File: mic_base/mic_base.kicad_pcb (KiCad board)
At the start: 2 copper layers, 50 x 50 mm, 25 parts, among them IC1 1512P08-U, J1 +Power-, J2 +Out-, J3 -Gain+, J4 +Mic In-, U1 NMA0515SC

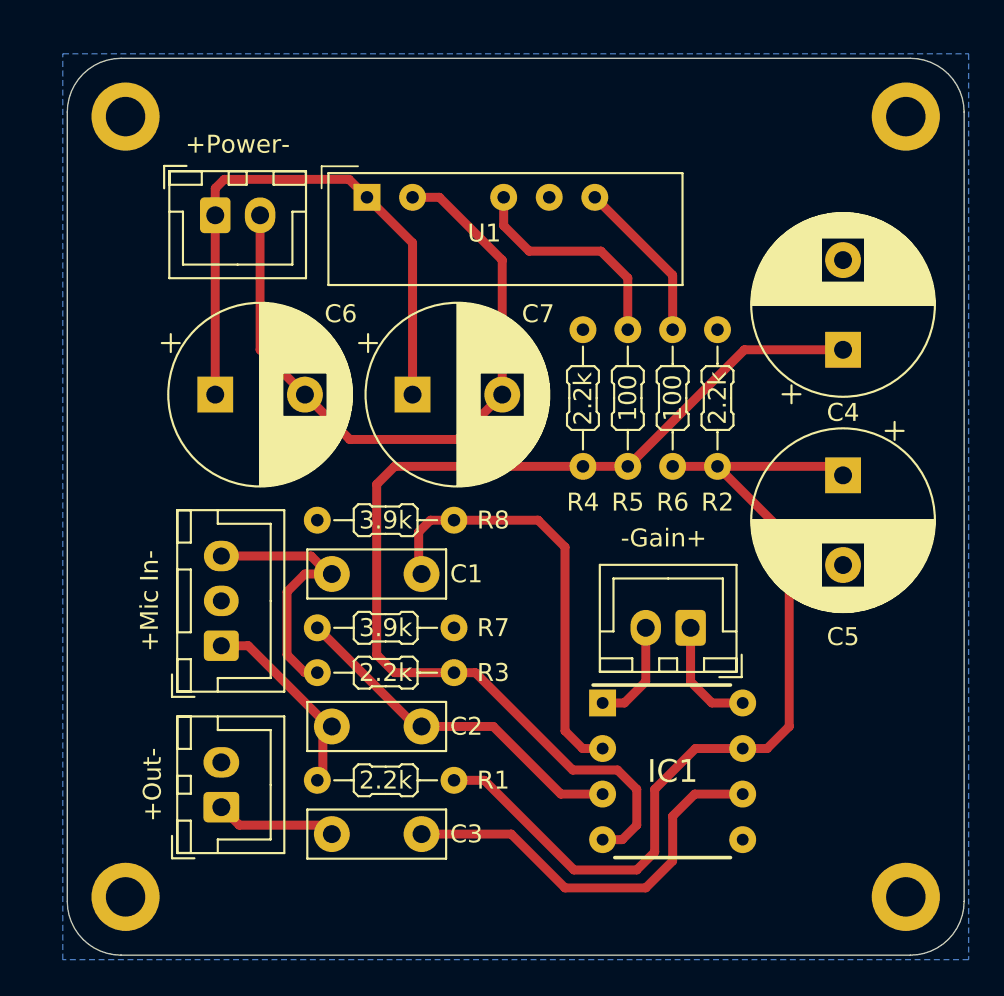
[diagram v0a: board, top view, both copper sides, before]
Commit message: moved capacitors, made pcb smaller
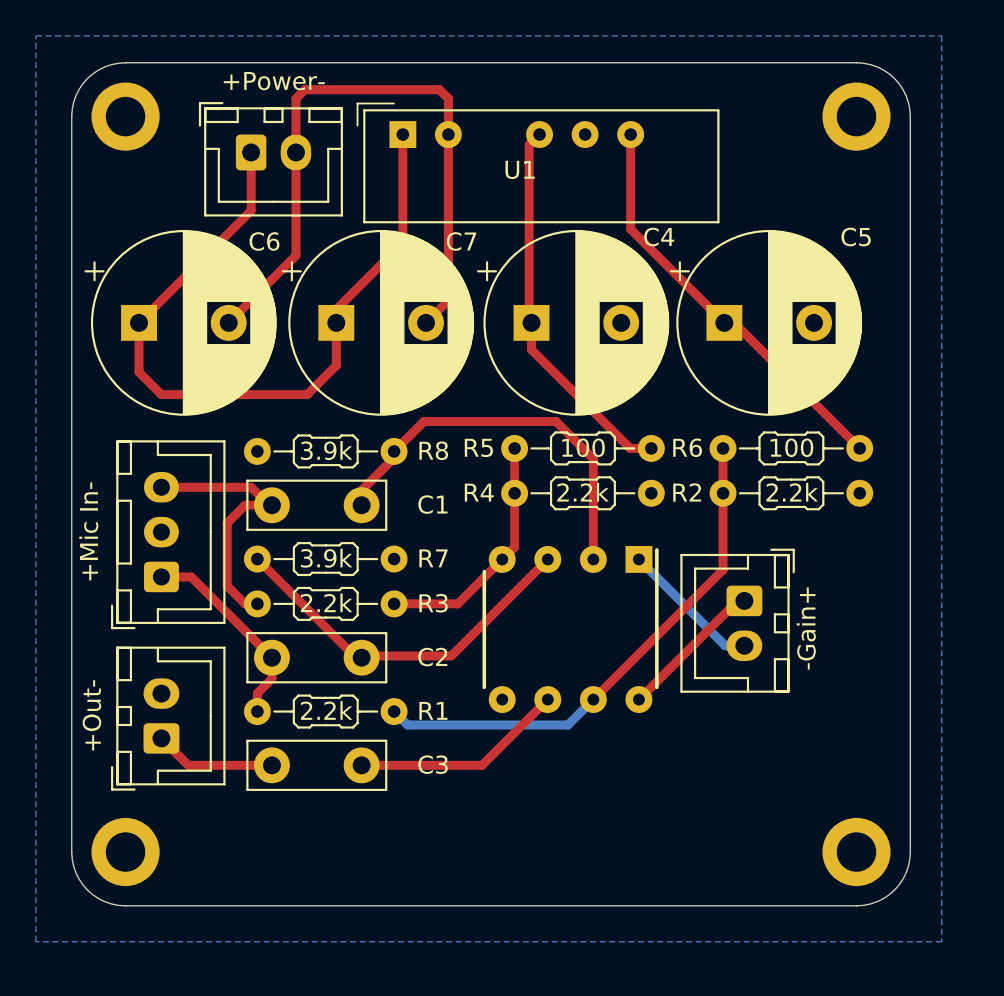
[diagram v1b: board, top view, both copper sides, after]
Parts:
- moved C4 17.4 mm to (104.6, 59.0), turned to 0 degrees
- moved R2 12.1 mm to (122.9, 68.5), turned to 180 degrees
- moved C5 10.8 mm to (115.4, 59.0), turned to 0 degrees
- moved R4 9.88 mm to (111.3, 68.5), turned to 180 degrees
- moved IC1 9.74 mm to (106.8, 76.1), turned to -90 degrees
- moved R5 6.39 mm to (103.7, 66.0), turned to 0 degrees
- moved C6 5.84 mm to (82.8, 59.0)
- moved C7 5.84 mm to (93.8, 59.0)
- moved R8 5.08 mm to (89.3, 66.2)
- moved C1 5.08 mm to (90.2, 69.2)
- moved C2 5.08 mm to (95.2, 77.7)
- moved C3 5.08 mm to (90.2, 83.7)
- moved J2 5.08 mm to (84.0, 82.2)
- moved J4 5.08 mm to (84.0, 73.2)
- moved R1 5.08 mm to (89.4, 80.7)
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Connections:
- C4 pad 1: /-VOut -> Net-(U1-VOUT-)
- C5 pad 1: /+VOut -> Net-(U1-VOUT+)
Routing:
- net /-VOut: track 60.5 -> 13.5 mm
- net /+VOut: track 52.3 -> 29.0 mm
- net Net-(U1-VOUT+): track 9.18 -> 23.1 mm
- net Net-(IC1-OUT): track 22.8 -> 11.9 mm
- net Net-(U1-VOUT-): track 12.6 -> 21.1 mm
- net /+5: track 32.7 -> 40.7 mm
- net /AGND: track 38.6 -> 36.0 mm
- net /-Gain: track 5.90 -> 7.87 mm
- net Net-(IC1--IN): track 24.1 -> 22.2 mm
- net /+Gain: track 6.40 -> 8.16 mm
- net /Out: track 6.07 -> 6.78 mm
- net Net-(IC1-+IN): track 19.7 -> 20.4 mm
- net /+Mic: track 10.7 -> 11.4 mm
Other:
- board size 50 x 50 mm -> 46.8 x 47 mm

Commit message: added images and readme
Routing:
- net Net-(U1-VOUT-): track 21.1 -> 20.4 mm

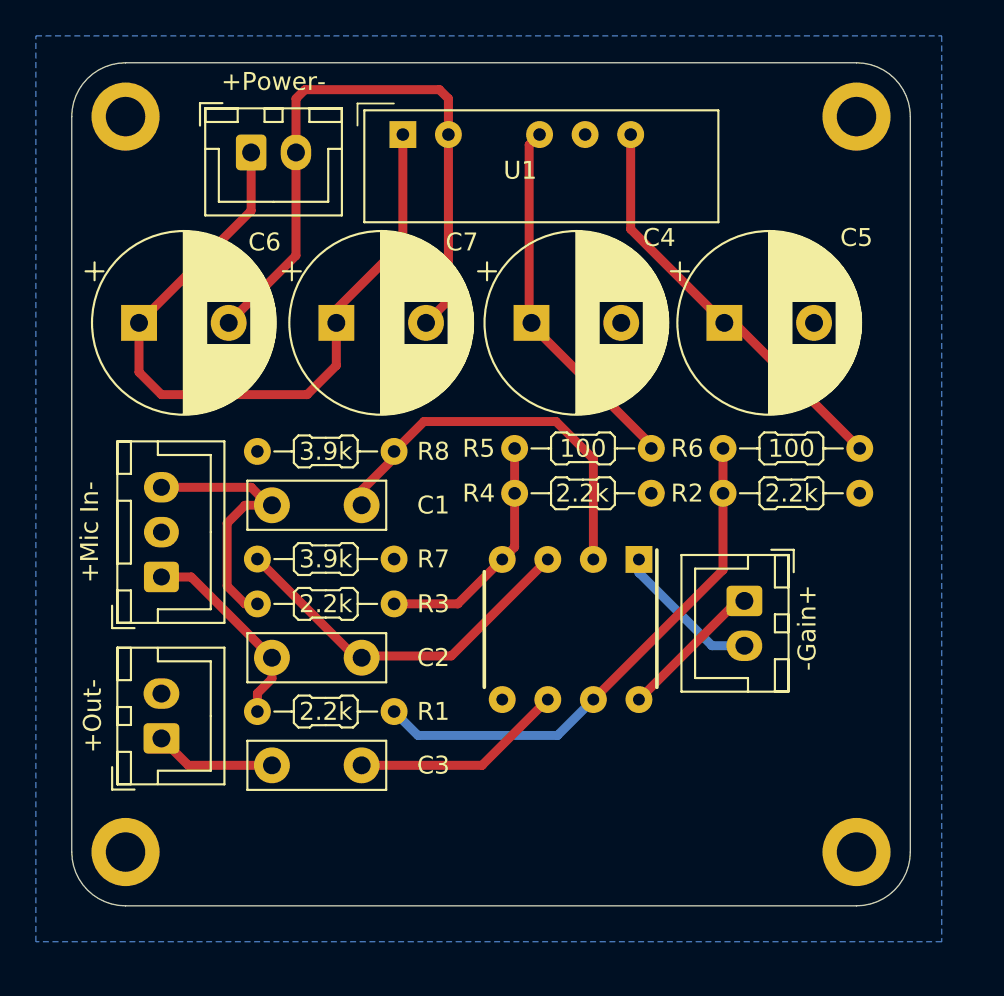
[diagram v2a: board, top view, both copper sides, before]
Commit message: changed resistors pin pitch from 7 to 5, compressed the board more
readme to be updated
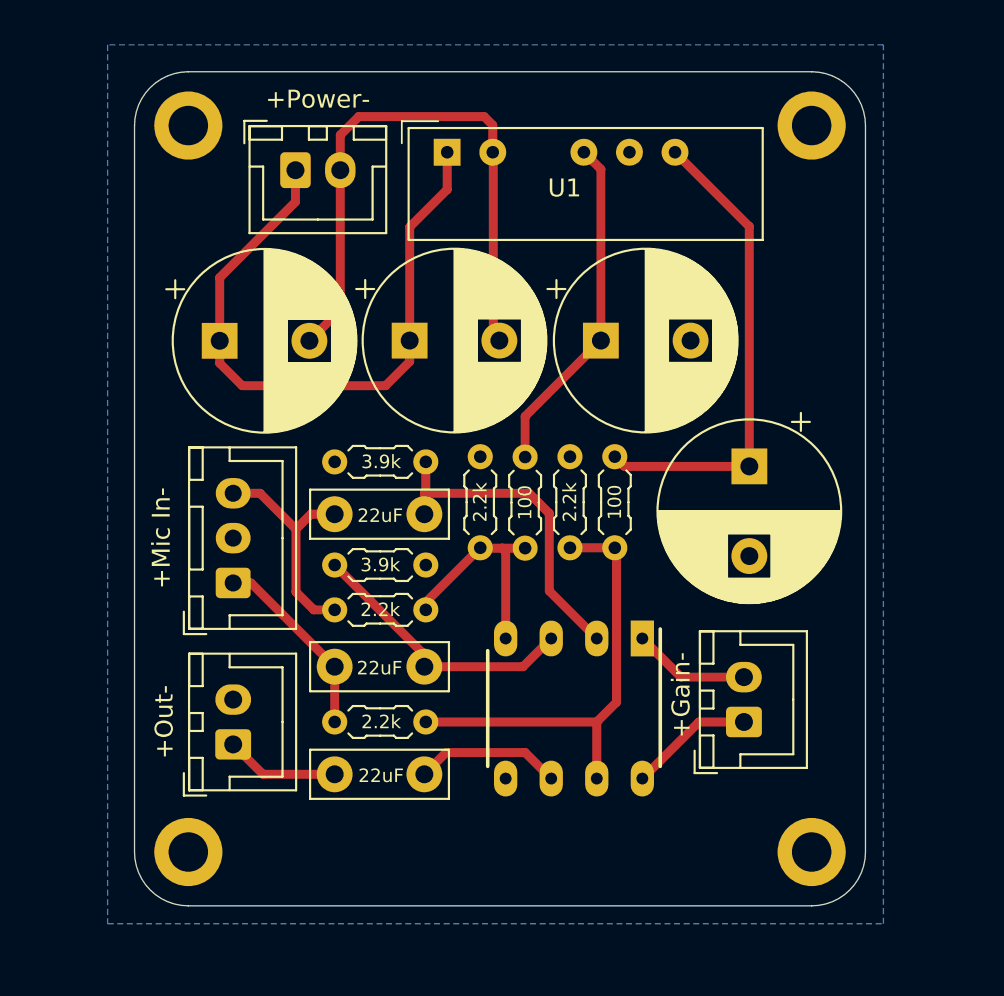
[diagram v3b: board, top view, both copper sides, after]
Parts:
- J3: value -Gain+ -> +Gain-
- R1, R2, R3, R4, R5, R6, R7, R8: footprint PCM_Resistor_THT_AKL:R_Axial_DIN0204_L3.6mm_D1.6mm_P7.62mm_Horizontal -> PCM_Resistor_THT_AKL:R_Axial_DIN0204_L3.6mm_D1.6mm_P5.08mm_Horizontal
- moved R2 16.3 mm to (106.8, 66.5), turned to -90 degrees
- moved R4 9.75 mm to (101.8, 66.5), turned to -90 degrees
- moved R6 8.19 mm to (109.3, 71.5), turned to 90 degrees
- moved C5 8.12 mm to (116.8, 67.0), turned to -90 degrees
- moved J3 6.75 mm to (116.5, 81.2), turned to 90 degrees
- moved R5 5.59 mm to (104.3, 71.6), turned to 90 degrees
- moved C6 4.61 mm to (87.2, 60.0)
- moved IC1 4.41 mm to (107.0, 80.5)
- moved R8 4.35 mm to (93.7, 66.8)
- moved R1 4.35 mm to (93.7, 81.2)
- moved C7 4.21 mm to (97.8, 60.0)
- moved J4 4.01 mm to (88.0, 73.5)
- moved J2 4.01 mm to (88.0, 82.5)
- moved C4 3.99 mm to (108.5, 60.0)
- moved H1 3.54 mm to (85.5, 48.0)
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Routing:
- net Net-(IC1-+IN): track 20.4 -> 15.5 mm
- net /+VOut: track 29.5 -> 25.4 mm
- net /+5: track 40.7 -> 36.7 mm
- net Net-(U1-VOUT+): track 23.1 -> 27.0 mm
- net Net-(IC1-OUT): track 11.9 -> 8.17 mm
- net Net-(IC1--IN): track 22.2 -> 19.6 mm
- net /AGND: track 36.0 -> 33.5 mm
- net /-Mic: track 15.0 -> 12.9 mm
- net /-Gain: track 8.31 -> 6.56 mm
- net Net-(U1-VOUT-): track 20.4 -> 19.1 mm
- net /-VOut: track 13.5 -> 12.3 mm
- net /+Gain: track 8.16 -> 6.97 mm
- net /+Mic: track 11.4 -> 10.7 mm
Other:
- board size 46.8 x 47 mm -> 40.8 x 46.5 mm

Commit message: changed footprints to 0805 smds, rewrote the readme
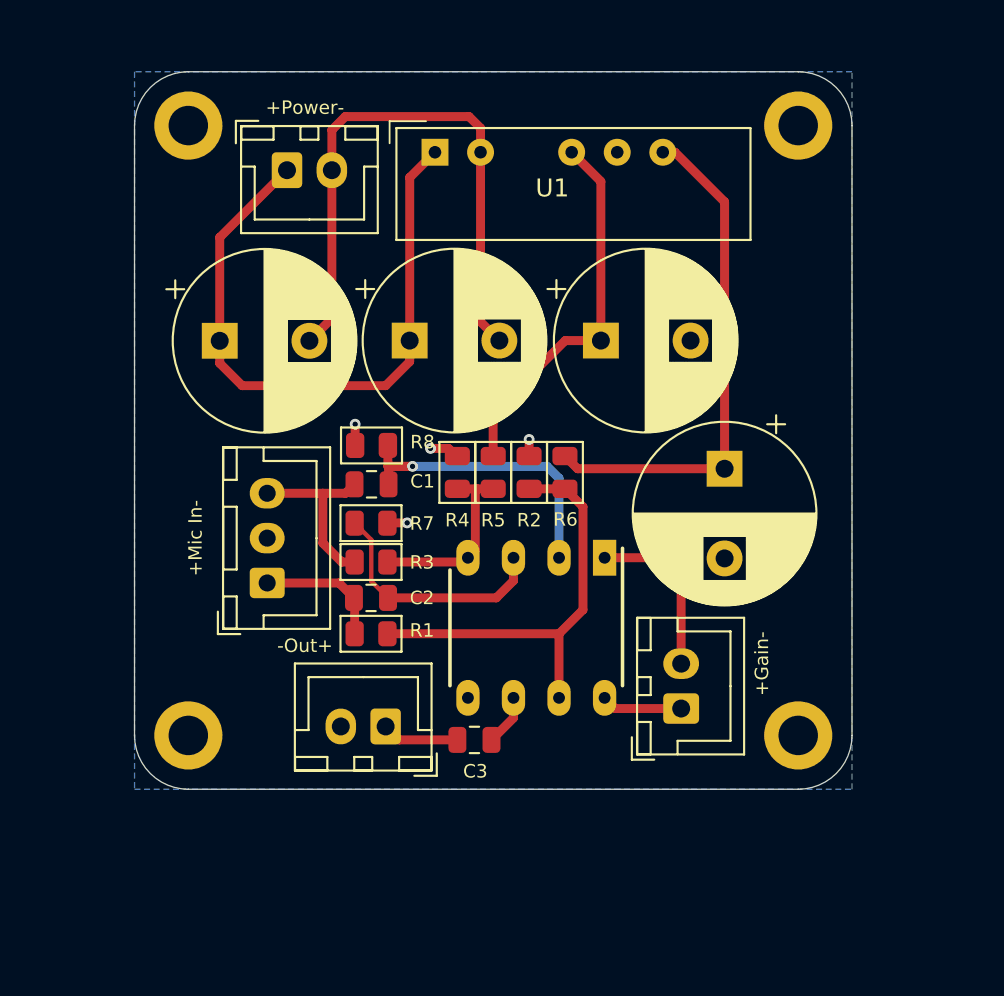
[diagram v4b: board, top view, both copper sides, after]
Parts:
- C1, C2, C3: footprint Capacitor_THT:C_Disc_D7.5mm_W2.5mm_P5.00mm -> Capacitor_SMD:C_0805_2012Metric
- J2: value +Out- -> -Out+
- R1, R2, R3, R4, R5, R6, R7, R8: footprint PCM_Resistor_THT_AKL:R_Axial_DIN0204_L3.6mm_D1.6mm_P5.08mm_Horizontal -> PCM_Resistor_SMD_AKL:R_0805_2012Metric
- moved J2 8.56 mm to (96.5, 81.5), turned to 180 degrees
- moved C3 8.02 mm to (101.5, 82.2)
- moved H4 6.54 mm to (119.5, 82.0)
- moved H3 6.50 mm to (85.5, 82.0)
- moved R1 5.32 mm to (95.7, 76.3)
- moved R6 5.04 mm to (106.5, 67.3)
- moved IC1 4.97 mm to (104.9, 76.0)
- moved C2 4.85 mm to (95.7, 74.3)
- moved R5 4.58 mm to (102.5, 67.3)
- moved R3 4.06 mm to (95.7, 72.3)
- moved R7 3.84 mm to (95.7, 70.2)
- moved J3 3.58 mm to (113.0, 80.5)
- moved C1 2.65 mm to (95.7, 68.0)
- moved R2 2.44 mm to (104.5, 67.3)
- moved R8 2.25 mm to (95.7, 65.8)
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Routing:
- net Net-(IC1-OUT): track 8.17 -> 2.85 mm
- net /GND: track 0.00 -> 4.96 mm, vias 0 -> 4
- net /+Mic: track 10.7 -> 7.20 mm
- net /-Gain: track 6.56 -> 9.66 mm
- net /-Mic: track 12.9 -> 10.1 mm
- net Net-(U1-VOUT-): track 19.1 -> 21.7 mm
- net /+Gain: track 6.97 -> 4.52 mm
- net /Out: track 6.35 -> 4.31 mm
- net Net-(IC1--IN): track 19.6 -> 17.8 mm, vias 0 -> 1
- net Net-(IC1-+IN): track 15.5 -> 13.6 mm
- net /-VOut: track 12.3 -> 10.6 mm
- net Net-(U1-VOUT+): track 27.0 -> 28.7 mm
- net /+VOut: track 25.4 -> 24.2 mm
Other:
- board size 40.8 x 46.5 mm -> 40 x 40 mm
